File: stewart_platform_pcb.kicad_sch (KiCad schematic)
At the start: 29 parts, among them J1 Conn_01x03, J2 Conn_01x03, J3 Conn_01x03, J4 Conn_01x03, J5 Conn_01x03, J6 Conn_01x03, J7 Conn_01x22, J8 Conn_01x22, U1 ESP32-S3-DevKitC

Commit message: Adding stepper drivers if needed/wanted. A4988 or TMC2209/TMC2208 compatible.
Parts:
- removed C8: C, symbol Device:C
- added A1, A2: Pololu_Breakout_A4988, Module:Pololu_Breakout-16_15.2x20.3mm, symbol Driver_Motor:Pololu_Breakout_A4988
- added C10, C8: 100nF, symbol Device:C_Small
- added H1, H2, H3, H4, H5, H6: MountingHole, MountingHole:MountingHole_3.2mm_M3, symbol Mechanical:MountingHole
- added J10: Fan Screw Terminal, TerminalBlock_Phoenix:TerminalBlock_Phoenix_MKDS-1,5-2_1x02_P5.00mm_Horizontal, symbol Connector:Screw_Terminal_01x02
- added J11: Conn_01x02, symbol Connector_Generic:Conn_01x02
- added J12, J13: Conn_01x04, symbol Connector_Generic:Conn_01x04
- added J9: Power Input, TerminalBlock_Phoenix:TerminalBlock_Phoenix_MKDS-1,5-2_1x02_P5.00mm_Horizontal, symbol Connector:Screw_Terminal_01x02
- added R13, R14, R15, R16: 22k, symbol Device:R_Small
- added SW1: SW_DIP_x04, Button_Switch_THT:SW_DIP_SPSTx04_Slide_9.78x12.34mm_W7.62mm_P2.54mm, symbol Switch:SW_DIP_x04
- J7, J8: footprint (none) -> Connector_PinHeader_2.54mm:PinHeader_1x22_P2.54mm_Vertical
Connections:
- net LIM_SW_1 is gone; now on net GPIO35: C1.1, R1.2, R2.1
- net LIM_SW_2 is gone; now on net GPIO36: C2.1, R3.2, R4.1
- net LIM_SW_3 is gone; now on net GPIO37: C3.1, R5.2, R6.1
- net LIM_SW_4 is gone; now on net GPIO38: C4.1, R7.2, R8.1
- net LIM_SW_5 is gone; now on net GPIO47: C5.1, R10.1, R9.2
- net LIM_SW_6 is gone; now on net GPIO48: C6.1, R11.2, R12.1
- net +3V3: now also A1.2 (VDD), A2.2 (VDD), C10.1, C8.1, SW1.1, SW1.2, SW1.3, SW1.4
- net +5V: no longer C7.1
- net EN/RESET: now also U1.3 (CHIP_PU)
- net GND: now also C7.2, J8.1 (Pin_1), J8.21 (Pin_21), J8.22 (Pin_22), U1.22 (GND), U1.23 (GND), U1.24 (GND), U1.44 (GND), A1.1 (GND), A1.7 (GND), A2.1 (GND), A2.7 (GND), C10.2, C8.2, J10.2 (Pin_2), J11.2 (Pin_2), J9.2 (Pin_2), R13.2, R14.2, R15.2, R16.2
- net GPIO10: now also U1.16 (GPIO10/ADC1_CH9)
- net GPIO11: now also U1.17 (GPIO11/ADC2_CH0)
- net GPIO12: now also U1.18 (GPIO12/ADC2_CH1)
- net GPIO13: now also U1.19 (GPIO13/ADC2_CH2)
- net GPIO14: now also U1.20 (GPIO14/ADC2_CH3)
- net GPIO15: now also U1.8 (GPIO15/ADC2_CH4/32K_P)
- net GPIO16: now also U1.9 (GPIO16/ADC2_CH5/32K_N)
- net GPIO17: now also U1.10 (GPIO17/ADC2_CH6)
- net GPIO18: now also U1.11 (GPIO18/ADC2_CH7)
- net GPIO3: now also U1.13 (GPIO3/ADC1_CH2)
- net GPIO4: now also U1.4 (GPIO4/ADC1_CH3)
- net GPIO46: now also U1.14 (GPIO46)
- net GPIO5: now also U1.5 (GPIO5/ADC1_CH4)
- net GPIO6: now also U1.6 (GPIO6/ADC1_CH5)
- net GPIO7: now also U1.7 (GPIO7/ADC1_CH6)
- net GPIO8: now also U1.12 (GPIO8/ADC1_CH7)
- net GPIO9: now also U1.15 (GPIO9/ADC1_CH8)
- net GPIO38: now reaches J8.10 (Pin_10)
- net GPIO38: now also U1.35 (GPIO38)
- net GPIO37: now reaches J8.11 (Pin_11)
- net GPIO37: now also U1.34 (GPIO37)
- net GPIO36: now reaches J8.12 (Pin_12)
- net GPIO36: now also U1.33 (GPIO36)
- net GPIO35: now reaches J8.13 (Pin_13)
- net GPIO35: now also U1.32 (GPIO35)
- net GPIO0: now reaches J8.14 (Pin_14)
- net GPIO0: now also U1.31 (GPIO0)
- net GPIO45: now reaches J8.15 (Pin_15)
- net GPIO45: now also U1.30 (GPIO45)
- net GPIO48: now reaches J8.16 (Pin_16)
- net GPIO48: now also U1.29 (GPIO48)
- net GPIO47: now reaches J8.17 (Pin_17)
- net GPIO47: now also U1.28 (GPIO47)
- net GPIO21: now reaches J8.18 (Pin_18)
- net GPIO21: now also U1.27 (GPIO21)
- net GPIO20: now reaches J8.19 (Pin_19)
- net GPIO20: now also U1.26 (GPIO20/USB_D+)
- net GPIO43/U0TXD: now reaches J8.2 (Pin_2)
- net GPIO43/U0TXD: now also U1.43 (GPIO43/U0TXD)
- net GPIO19: now reaches J8.20 (Pin_20)
- net GPIO19: now also U1.25 (GPIO19/USB_D-)
- net GPIO44/U0RXD: now reaches J8.3 (Pin_3)
- net GPIO44/U0RXD: now also U1.42 (GPIO44/U0RXD)
- net GPIO1: now reaches J8.4 (Pin_4)
- net GPIO1: now also U1.41 (GPIO1/ADC1_CH0)
- net GPIO2: now reaches J8.5 (Pin_5)
- net GPIO2: now also U1.40 (GPIO2/ADC1_CH1)
- net GPIO42/MTMS: now reaches J8.6 (Pin_6)
- net GPIO42/MTMS: now also U1.39 (GPIO42/MTMS)
- net GPIO41/MTDI: now reaches J8.7 (Pin_7)
- net GPIO41/MTDI: now also U1.38 (GPIO41/MTDI)
- net GPIO40/MTDO: now reaches J8.8 (Pin_8)
- net GPIO40/MTDO: now also U1.37 (GPIO40/MTDO)
- net GPIO39/MTCK: now reaches J8.9 (Pin_9)
- net GPIO39/MTCK: now also U1.36 (GPIO39/MTCK)
- new net: A2.10 (MS1), R13.1, SW1.5
- new net: A2.11 (MS2), R14.1, SW1.6
- new net: A1.11 (MS2), R15.1, SW1.7
- new net: A1.10 (MS1), R16.1, SW1.8
- new net: A1.3 (1B), J12.1 (Pin_1)
- new net: A1.4 (1A), J12.2 (Pin_2)
- new net: A1.5 (2A), J12.3 (Pin_3)
- new net: A1.6 (2B), J12.4 (Pin_4)
- new net: A2.3 (1B), J13.1 (Pin_1)
- new net: A2.4 (1A), J13.2 (Pin_2)
- new net: A2.5 (2A), J13.3 (Pin_3)
- new net: A2.6 (2B), J13.4 (Pin_4)
- new net +V_MOT: A1.8 (VMOT), A2.8 (VMOT), C7.1, J10.1 (Pin_1), J11.1 (Pin_1), J9.1 (Pin_1)
- new net M0_DIR: A1.16 (DIR)
- new net M0_STP: A1.15 (STEP)
- new net M1_DIR: A2.16 (DIR)
- new net M1_STP: A2.15 (STEP)
- new net MS3/SPRD/PDN/NC: A1.12 (MS3), A2.12 (MS3)
- new net ~ENABLE: A1.9 (~{ENABLE}), A2.9 (~{ENABLE})
- new net ~RESET/PDN_UART_1: A1.13 (~{RESET}), A2.13 (~{RESET})
- new net ~SLEEP/CLK: A1.14 (~{SLEEP}), A2.14 (~{SLEEP})
- no-connect marks 0 -> 2
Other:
- note added: "Bootloader pins: 0,3,45,46"
- note added: "MS0/MS1 address sel. for UART"
- note added: "Microstepping for non-UART"
- note added: "Note to self: Label motors as M0-M5 & Axes XYZABC"
- moved on the sheet: J7, J8, U1

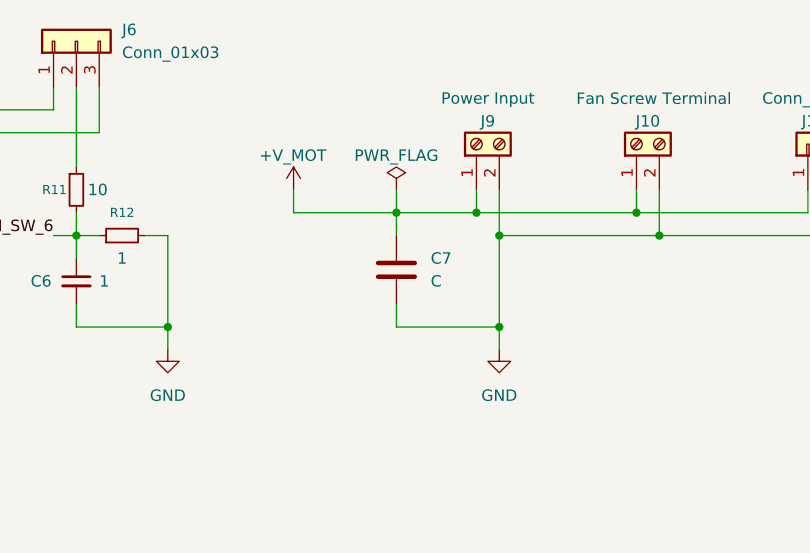
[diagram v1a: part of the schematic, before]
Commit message: PCB 2 x Stepper Drivers
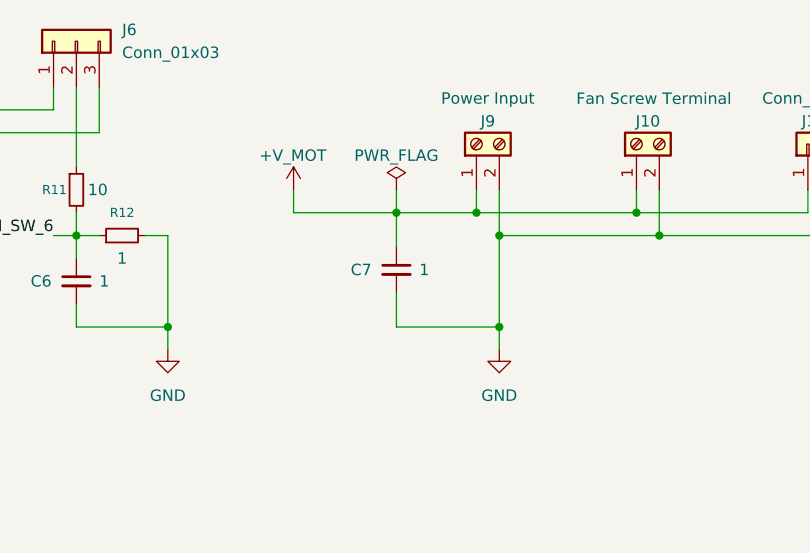
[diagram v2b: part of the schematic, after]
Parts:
- removed C7: C, symbol Device:C
- added C7: 1, symbol Device:C_Small
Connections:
- net +V_MOT: now also C7.1
- net GND: now also C7.2
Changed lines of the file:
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@@
 	(wire
 		(pts
-			(xy 213.36 41.91) (xy 213.36 44.45)
+			(xy 213.36 41.91) (xy 213.36 45.72)
 		)
 		(stroke
@@
 	(wire
 		(pts
-			(xy 213.36 54.61) (xy 213.36 52.07)
-		)
-		(stroke
-			(width 0)
-			(type default)
-		)
-	)
-	(wire
-		(pts
 			(xy 139.7 142.24) (xy 144.78 142.24)
 		)
@@
 	(wire
 		(pts
+			(xy 213.36 50.8) (xy 213.36 54.61)
+		)
+		(stroke
+			(width 0)
+			(type default)
+		)
+	)
+	(wire
+		(pts
 			(xy 72.39 127) (xy 77.47 127)
 		)
@@
 	)
 	(symbol
+		(lib_id "Device:C_Small")
+		(at 213.36 48.26 0)
+		(unit 1)
+		(exclude_from_sim no)
+		(in_bom yes)
+		(on_board yes)
+		(dnp no)
+		(property "Reference" "C7"
+			(at 208.28 48.26 0)
+			(effects
+				(font
+					(size 1.27 1.27)
+				)
+				(justify left)
+			)
+		)
+		(property "Value" "1"
+			(at 215.9 48.26 0)
+			(effects
+				(font
+					(size 1.27 1.27)
+				)
+				(justify left)
+			)
+		)
+		(property "Footprint" ""
+			(at 213.36 48.26 0)
+			(effects
+				(font
+					(size 1.27 1.27)
+				)
+				(hide yes)
+			)
+		)
+		(property "Datasheet" "~"
+			(at 213.36 48.26 0)
+			(effects
+				(font
+					(size 1.27 1.27)
+				)
+				(hide yes)
+			)
+		)
+		(property "Description" "Unpolarized capacitor, small symbol"
+			(at 213.36 48.26 0)
+			(effects
+				(font
+					(size 1.27 1.27)
+				)
+				(hide yes)
+			)
+		)
+		(pin "1"
+		)
+		(pin "2"
+		)
+		(instances
+			(project "stewart_platform_pcb"
+				(path "/674f121c-3722-4a2f-ad96-6128bc84c507"
+					(reference "C7")
+					(unit 1)
+				)
+			)
+		)
+	)
+	(symbol
 		(lib_id "power:GND")
 		(at 288.29 234.95 0)
@@
 					(unit 1)
 				)
-			)
-		)
-	)
-	(symbol
-		(lib_id "Device:C")
-		(at 213.36 48.26 0)
-		(unit 1)
-		(exclude_from_sim no)
-		(in_bom yes)
-		(on_board yes)
-		(dnp no)
-		(fields_autoplaced yes)
-		(property "Reference" "C7"
-			(at 217.17 46.9899 0)
-			(effects
-				(font
-					(size 1.27 1.27)
-				)
-				(justify left)
-			)
-		)
-		(property "Value" "C"
-			(at 217.17 49.5299 0)
-			(effects
-				(font
-					(size 1.27 1.27)
-				)
-				(justify left)
-			)
-		)
-		(property "Footprint" ""
-			(at 214.3252 52.07 0)
-			(effects
-				(font
-					(size 1.27 1.27)
-				)
-				(hide yes)
-			)
-		)
-		(property "Datasheet" "~"
-			(at 213.36 48.26 0)
-			(effects
-				(font
-					(size 1.27 1.27)
-				)
-				(hide yes)
-			)
-		)
-		(property "Description" "Unpolarized capacitor"
-			(at 213.36 48.26 0)
-			(effects
-				(font
-					(size 1.27 1.27)
-				)
-				(hide yes)
-			)
-		)
-		(pin "2"
-		)
-		(pin "1"
-		)
-		(instances
-			(project "stewart_platform_pcb"
-				(path "/674f121c-3722-4a2f-ad96-6128bc84c507"
-					(reference "C7")
-					(unit 1)
-				)

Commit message: Updates
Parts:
- added A3, A4, A5, A6: Pololu_Breakout_A4988, Module:Pololu_Breakout-16_15.2x20.3mm, symbol Driver_Motor:Pololu_Breakout_A4988
- added C11, C18, C19, C9: 100nF, Capacitor_THT:C_Disc_D4.3mm_W1.9mm_P5.00mm, symbol Device:C_Small
- added C12, C13, C14, C15, C16, C17: 220uF, Capacitor_THT:C_Radial_D10.0mm_H12.5mm_P5.00mm, symbol Device:C
- added J14, J15, J16, J17, J18, J19, J20, J21, J22, J23: Conn_01x04, Connector_Molex:Molex_KK-254_AE-6410-04A_1x04_P2.54mm_Vertical, symbol Connector_Generic:Conn_01x04
- added J24, J25, J26, J27, J28, J29: Conn_01x02, Connector_Molex:Molex_KK-254_AE-6410-02A_1x02_P2.54mm_Vertical, symbol Connector_Generic:Conn_01x02
- added J30, J31, J32, J33, J34, J35: Conn_01x06, Connector_Molex:Molex_KK-254_AE-6410-06A_1x06_P2.54mm_Vertical, symbol Connector_Generic:Conn_01x06
- added R17, R18, R19, R20, R21, R22, R23, R24: 22k, Resistor_THT:R_Axial_DIN0207_L6.3mm_D2.5mm_P7.62mm_Horizontal, symbol Device:R_Small
- added SW2, SW3: SW_DIP_x04, Button_Switch_THT:SW_DIP_SPSTx04_Slide_9.78x12.34mm_W7.62mm_P2.54mm, symbol Switch:SW_DIP_x04
- C10, C8: footprint (none) -> Capacitor_THT:C_Disc_D4.3mm_W1.9mm_P5.00mm
- J1, J2, J3, J4, J5, J6: footprint (none) -> Connector_Molex:Molex_KK-254_AE-6410-03A_1x03_P2.54mm_Vertical
- J11: footprint (none) -> Connector_Molex:Molex_KK-254_AE-6410-02A_1x02_P2.54mm_Vertical
- J12, J13: footprint (none) -> Connector_Molex:Molex_KK-254_AE-6410-04A_1x04_P2.54mm_Vertical
- R1, R10, R11, R12, R13, R14, R15, R16, R2, R3, R4, R5, R6, R7, R8, R9: footprint (none) -> Resistor_THT:R_Axial_DIN0207_L6.3mm_D2.5mm_P7.62mm_Horizontal
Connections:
- net +3V3: now also A3.2 (VDD), A4.2 (VDD), A5.2 (VDD), A6.2 (VDD), C11.1, C18.1, C19.1, C9.1, J24.1 (Pin_1), J25.1 (Pin_1), J26.1 (Pin_1), J27.1 (Pin_1), J28.1 (Pin_1), J29.1 (Pin_1), SW2.1, SW2.2, SW2.3, SW2.4
- net +V_MOT: now also A3.8 (VMOT), A4.8 (VMOT), A5.8 (VMOT), A6.8 (VMOT), C12.1, C13.1, C14.1, C15.1, C16.1, C17.1
- net GND: now also A3.1 (GND), A3.7 (GND), A4.1 (GND), A4.7 (GND), A5.1 (GND), A5.7 (GND), A6.1 (GND), A6.7 (GND), C11.2, C12.2, C13.2, C14.2, C15.2, C16.2, C17.2, C18.2, C19.2, C9.2, J30.2 (Pin_2), J30.4 (Pin_4), J30.6 (Pin_6), J31.2 (Pin_2), J31.4 (Pin_4), J31.6 (Pin_6), J32.2 (Pin_2), J32.4 (Pin_4), J32.6 (Pin_6), J33.2 (Pin_2), J33.4 (Pin_4), J33.6 (Pin_6), J34.2 (Pin_2), J34.4 (Pin_4), J34.6 (Pin_6), J35.2 (Pin_2), J35.4 (Pin_4), J35.6 (Pin_6), R17.2, R18.2, R19.2, R20.2, R21.2, R22.1, R23.1, R24.2
- net M0_DIR: now also J30.3 (Pin_3)
- net M0_STP: now also J30.5 (Pin_5)
- net M1_DIR: now also J31.3 (Pin_3)
- net M1_STP: now also J31.5 (Pin_5)
- net ~ENABLE: now also A3.9 (~{ENABLE}), A4.9 (~{ENABLE}), A5.9 (~{ENABLE}), A6.9 (~{ENABLE}), J30.1 (Pin_1), J31.1 (Pin_1), J32.1 (Pin_1), J33.1 (Pin_1), J34.1 (Pin_1), J35.1 (Pin_1)
- net ~RESET/PDN_UART_1: now also A3.13 (~{RESET}), A4.13 (~{RESET}), A6.13 (~{RESET}); no longer A1.13 (~{RESET}), A2.13 (~{RESET})
- net ~SLEEP/CLK: now also A3.14 (~{SLEEP}), A4.14 (~{SLEEP}), A5.14 (~{SLEEP}), A6.14 (~{SLEEP})
- net at J2.2 (Pin_2), R3.1: now also J25.2 (Pin_2)
- net at J1.2 (Pin_2), R1.1: now also J24.2 (Pin_2)
- net at J6.2 (Pin_2), R11.1: now also J29.2 (Pin_2)
- net at J3.2 (Pin_2), R5.1: now also J26.2 (Pin_2)
- net at A1.11 (MS2), R15.1: now also SW1.8; no longer SW1.7
- net at A1.10 (MS1), R16.1: now also SW1.7; no longer SW1.8
- net M0_1B: now reaches A1.3 (1B), J12.1 (Pin_1)
- net M0_1B: now also J17.1 (Pin_1)
- net M0_1A: now reaches A1.4 (1A), J12.2 (Pin_2)
- net M0_1A: now also J17.2 (Pin_2)
- net M0_2A: now reaches A1.5 (2A), J12.3 (Pin_3)
- net M0_2A: now also J17.3 (Pin_3)
- net M0_2B: now reaches A1.6 (2B), J12.4 (Pin_4)
- net M0_2B: now also J17.4 (Pin_4)
- net M1_1B: now reaches A2.3 (1B), J13.1 (Pin_1)
- net M1_1B: now also J16.1 (Pin_1)
- net M1_1A: now reaches A2.4 (1A), J13.2 (Pin_2)
- net M1_1A: now also J16.2 (Pin_2)
- net M1_2A: now reaches A2.5 (2A), J13.3 (Pin_3)
- net M1_2A: now also J16.3 (Pin_3)
- net M1_2B: now reaches A2.6 (2B), J13.4 (Pin_4)
- net M1_2B: now also J16.4 (Pin_4)
- net at J5.2 (Pin_2), R9.1: now also J28.2 (Pin_2)
- net at J4.2 (Pin_2), R7.1: now also J27.2 (Pin_2)
- net MS3/SPRD/PDN/NC renamed MS3/SPRD/PDN_UART_0/NC
- net MS3/SPRD/PDN_UART_0/NC: now also A5.12 (MS3)
- new net: A4.11 (MS2), R19.1, SW2.8
- new net: A5.11 (MS2), R21.1, SW3.6
- new net: A3.10 (MS1), R17.1, SW2.5
- new net: A3.11 (MS2), R18.1, SW2.6
- new net: A4.10 (MS1), R20.1, SW2.7
- new net: A5.10 (MS1), R22.2, SW3.5
- new net: A6.10 (MS1), R23.2, SW3.7
- new net: A6.11 (MS2), R24.1, SW3.8
- new net M2_1A: A4.4 (1A), J15.2 (Pin_2), J19.2 (Pin_2)
- new net M2_1B: A4.3 (1B), J15.1 (Pin_1), J19.1 (Pin_1)
- new net M2_2A: A4.5 (2A), J15.3 (Pin_3), J19.3 (Pin_3)
- new net M2_2B: A4.6 (2B), J15.4 (Pin_4), J19.4 (Pin_4)
- new net M2_DIR: A4.16 (DIR), J32.5 (Pin_5)
- new net M2_STP: A4.15 (STEP), J32.3 (Pin_3)
- new net M3_1A: A3.4 (1A), J14.2 (Pin_2), J18.2 (Pin_2)
- new net M3_1B: A3.3 (1B), J14.1 (Pin_1), J18.1 (Pin_1)
- new net M3_2A: A3.5 (2A), J14.3 (Pin_3), J18.3 (Pin_3)
- new net M3_2B: A3.6 (2B), J14.4 (Pin_4), J18.4 (Pin_4)
- new net M3_DIR: A3.16 (DIR), J33.5 (Pin_5)
- new net M3_STP: A3.15 (STEP), J33.3 (Pin_3)
- new net M4_1A: A5.4 (1A), J20.2 (Pin_2), J21.2 (Pin_2)
- new net M4_1B: A5.3 (1B), J20.1 (Pin_1), J21.1 (Pin_1)
- new net M4_2A: A5.5 (2A), J20.3 (Pin_3), J21.3 (Pin_3)
- new net M4_2B: A5.6 (2B), J20.4 (Pin_4), J21.4 (Pin_4)
- new net M4_DIR: A5.16 (DIR), J34.5 (Pin_5)
- new net M4_STP: A5.15 (STEP), J34.3 (Pin_3)
- new net M5_1A: A6.4 (1A), J22.2 (Pin_2), J23.2 (Pin_2)
- new net M5_1B: A6.3 (1B), J22.1 (Pin_1), J23.1 (Pin_1)
- new net M5_2A: A6.5 (2A), J22.3 (Pin_3), J23.3 (Pin_3)
- new net M5_2B: A6.6 (2B), J22.4 (Pin_4), J23.4 (Pin_4)
- new net M5_DIR: A6.16 (DIR), J35.5 (Pin_5)
- new net M5_STP: A6.15 (STEP), J35.3 (Pin_3)
- new net MS3/SPRD/PDN_UART_1/NC: A3.12 (MS3), A4.12 (MS3), A6.12 (MS3)
- new net ~RESET/PDN_UART_0: A1.13 (~{RESET}), A2.13 (~{RESET}), A5.13 (~{RESET})
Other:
- note added: "PDN_UART/PDN need 1kOhm resistor"
- moved on the sheet: A1, A2, C1, C10, C2, C3, C4, C5, C6, C7, C8, H1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

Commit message: Before rotations
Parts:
- C1, C2, C3, C4, C5, C6: value 1 -> 2.2uF; footprint (none) -> Capacitor_THT:C_Radial_D6.3mm_H5.0mm_P2.50mm
- J1, J2, J3, J4, J5, J6: footprint Connector_Molex:Molex_KK-254_AE-6410-03A_1x03_P2.54mm_Vertical -> Connector_JST:JST_XH_B3B-XH-A_1x03_P2.50mm_Vertical
- J11, J24, J25, J26, J27, J28, J29: footprint Connector_Molex:Molex_KK-254_AE-6410-02A_1x02_P2.54mm_Vertical -> Connector_JST:JST_XH_B2B-XH-A_1x02_P2.50mm_Vertical
- J12, J13, J14, J15, J16, J17, J18, J19, J20, J21, J22, J23: footprint Connector_Molex:Molex_KK-254_AE-6410-04A_1x04_P2.54mm_Vertical -> Connector_JST:JST_XH_B4B-XH-A_1x04_P2.50mm_Vertical
- J30, J31, J32, J33, J34, J35: footprint Connector_Molex:Molex_KK-254_AE-6410-06A_1x06_P2.54mm_Vertical -> Connector_JST:JST_XH_B6B-XH-A_1x06_P2.50mm_Vertical
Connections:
- net +3V3: now also SW3.1, SW3.2, SW3.3, SW3.4
- net GPIO35: now also C2.1, R3.2, R4.1; no longer C1.1, R1.2, R2.1
- net GPIO36: now also C3.1, R5.2, R6.1; no longer C2.1, R3.2, R4.1
- net GPIO37: now also C4.1, R7.2, R8.1; no longer C3.1, R5.2, R6.1
- net GPIO38: now also C5.1, R10.1, R9.2; no longer C4.1, R7.2, R8.1
- net GPIO47: now also C6.1, R11.2, R12.1; no longer C5.1, R10.1, R9.2
- net GPIO48: no longer C6.1, R11.2, R12.1
- net M2_DIR: now also J32.3 (Pin_3); no longer J32.5 (Pin_5)
- net M2_STP: now also J32.5 (Pin_5); no longer J32.3 (Pin_3)
- net M3_DIR: now also J33.3 (Pin_3); no longer J33.5 (Pin_5)
- net M3_STP: now also J33.5 (Pin_5); no longer J33.3 (Pin_3)
- net M4_DIR: now also J34.3 (Pin_3); no longer J34.5 (Pin_5)
- net M4_STP: now also J34.5 (Pin_5); no longer J34.3 (Pin_3)
- net M5_DIR: now also J35.3 (Pin_3); no longer J35.5 (Pin_5)
- net M5_STP: now also J35.5 (Pin_5); no longer J35.3 (Pin_3)
- net at A5.11 (MS2), R21.1: now also SW3.8; no longer SW3.6
- net at A5.10 (MS1), R22.2: now also SW3.7; no longer SW3.5
- net at A6.10 (MS1), R23.2: now also SW3.5; no longer SW3.7
- net at A6.11 (MS2), R24.1: now also SW3.6; no longer SW3.8
- new net LIM_SW_0: C1.1, R1.2, R2.1
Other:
- moved on the sheet: R21, R22, R23, R24
